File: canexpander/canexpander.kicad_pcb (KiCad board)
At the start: 2 copper layers, 8 parts, among them J1 CocobotCAN, J2 CocobotCAN, J3 CocobotCAN, J4 CocobotCAN, J5 CocobotCAN, J6 Conn_01x01, J7 Conn_01x01

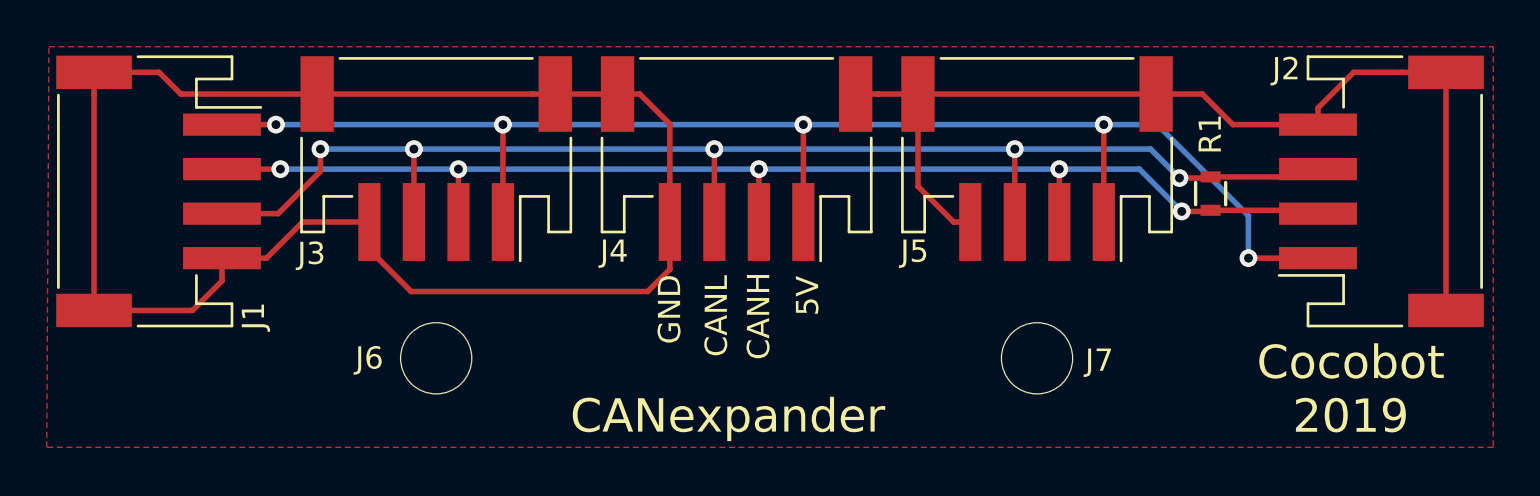
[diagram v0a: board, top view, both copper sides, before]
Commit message: Add protection diodes on CANexpander board
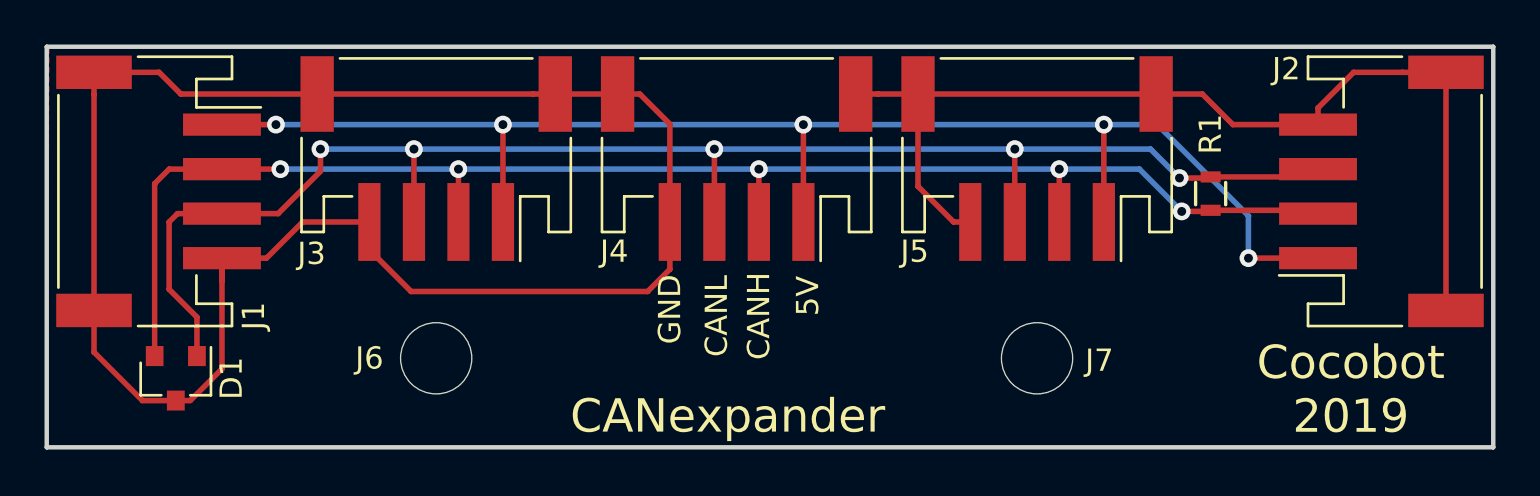
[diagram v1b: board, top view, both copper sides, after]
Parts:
- added D1: NUP2105LT1G, espitall:SOT-23, F.Cu at (55.8, 64.9)
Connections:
- J6 pad 1: (no net) -> Net-(J6-Pad1)
- J7 pad 1: (no net) -> Net-(J7-Pad1)
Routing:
- net Net-(D1-Pad2): track 57.2 -> 68.3 mm
- net Net-(D1-Pad1): track 61.6 -> 70.6 mm
- net GND: track 121.0 -> 128.8 mm
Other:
- board outline added: 65 x 18 mm

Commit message: add step on gitignore
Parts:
- added J8: CocobotCAN, espitall:JST_PH_S5B-PH-SM4-TB_05x2.00mm_Angled, B.Cu at (85.0, 55.0)
- J1, J2, J3, J5: footprint espitall:JST_PH_S4B-PH-SM4-TB_04x2.00mm_Angled -> espitall:JST_PH_S5B-PH-SM4-TB_05x2.00mm_Angled
- J4: footprint espitall:JST_PH_S4B-PH-SM4-TB_04x2.00mm_Angled -> espitall:JST_PH_S5B-PH-SM4-TB_05x2.00mm_Angled; moved to B.Cu
- moved R1 12.2 mm to (91.0, 61.1)
- moved J4 12.0 mm to (69.0, 55.0), turned to 0 degrees
- moved J2 11.1 mm to (99.0, 58.0)
- moved J5 9.50 mm to (85.0, 55.0)
- moved J7 7.50 mm to (87.0, 64.0)
- moved D1 5.23 mm to (61.0, 65.5), turned to 0 degrees
- moved J1 1.50 mm to (55.0, 58.0)
- moved J3 1.50 mm to (69.0, 55.0)
- moved J6 0.50 mm to (67.0, 64.0)
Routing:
- net GND: track 128.8 -> 184.7 mm, vias 0 -> 8
- net Net-(D1-Pad2): track 68.3 -> 92.6 mm, vias 5 -> 3
- net Net-(J1-Pad1): track 66.0 -> 84.2 mm, vias 5 -> 3
- net Net-(D1-Pad1): track 70.6 -> 74.4 mm, vias 5 -> 3
- added copper zone on B.Cu, net GND
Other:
- board size 65 x 18 mm -> 54 x 18 mm
- board text removed: "5V"
- board text removed: "CANH"
- board text removed: "CANL"
- board text removed: "GND"
